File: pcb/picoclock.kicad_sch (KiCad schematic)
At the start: 67 parts, among them J1 UART, J10 USB, J11 Alt Power, J12 PWM, J13 AUDIO, J2 AUDIO, J3 xx, J4 xx, J5 Micro_SD_Card_Det1, J6 USB_C_Receptacle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

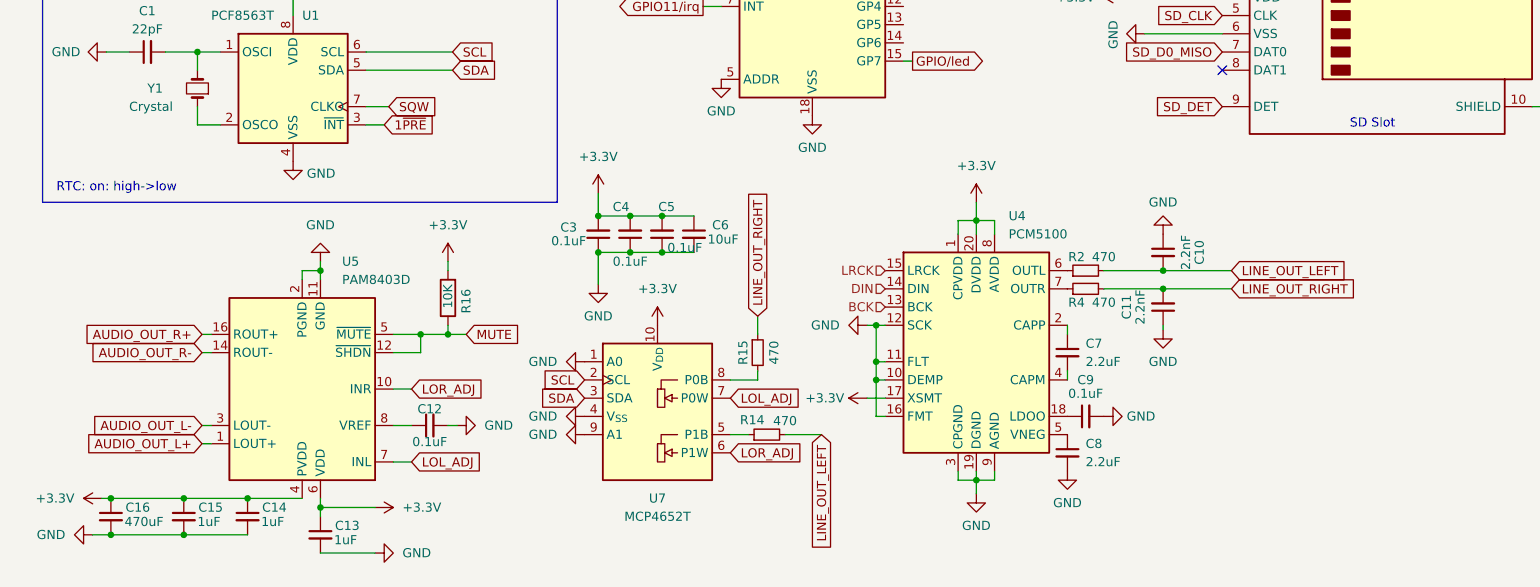
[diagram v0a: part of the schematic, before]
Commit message: [pcb] audio circuit fixes
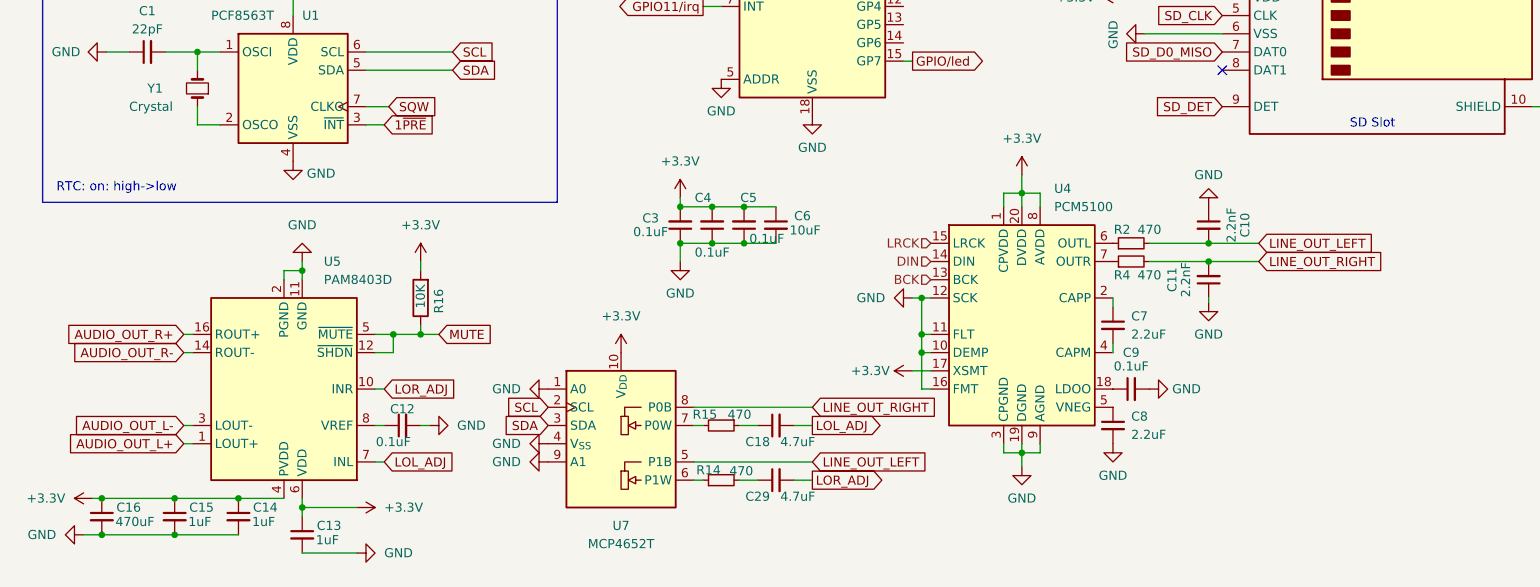
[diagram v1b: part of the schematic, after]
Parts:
- added C18, C29: 4.7uF, Capacitor_SMD:C_0603_1608Metric, symbol Device:C_Small
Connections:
- net LINE_OUT_LEFT: now also U7.5 (P1B); no longer R14.2
- net LINE_OUT_RIGHT: now also U7.8 (P0B); no longer R15.1
- net LOL_ADJ: now also C18.2; no longer U7.7 (P0W)
- net LOR_ADJ: now also C29.2; no longer U7.6 (P1W)
- net at R15.2: now also U7.7 (P0W); no longer U7.8 (P0B)
- net at R14.1: now also U7.6 (P1W); no longer U7.5 (P1B)
- new net: C18.1, R15.1
- new net: C29.1, R14.2
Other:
- moved on the sheet: C10, C11, C12, C13, C14, C15, C16, C3, C4, C5, C6, C7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

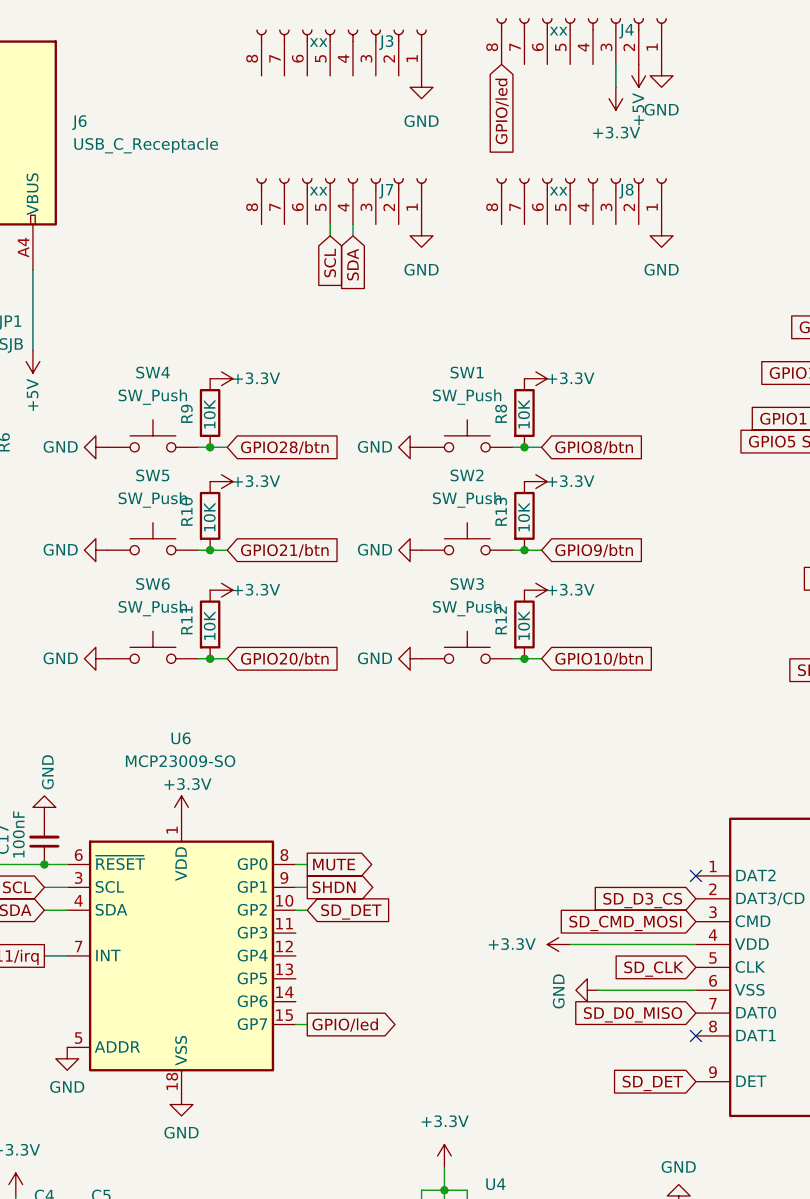
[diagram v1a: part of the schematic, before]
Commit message: [pcb] fpc screen connector at the right place
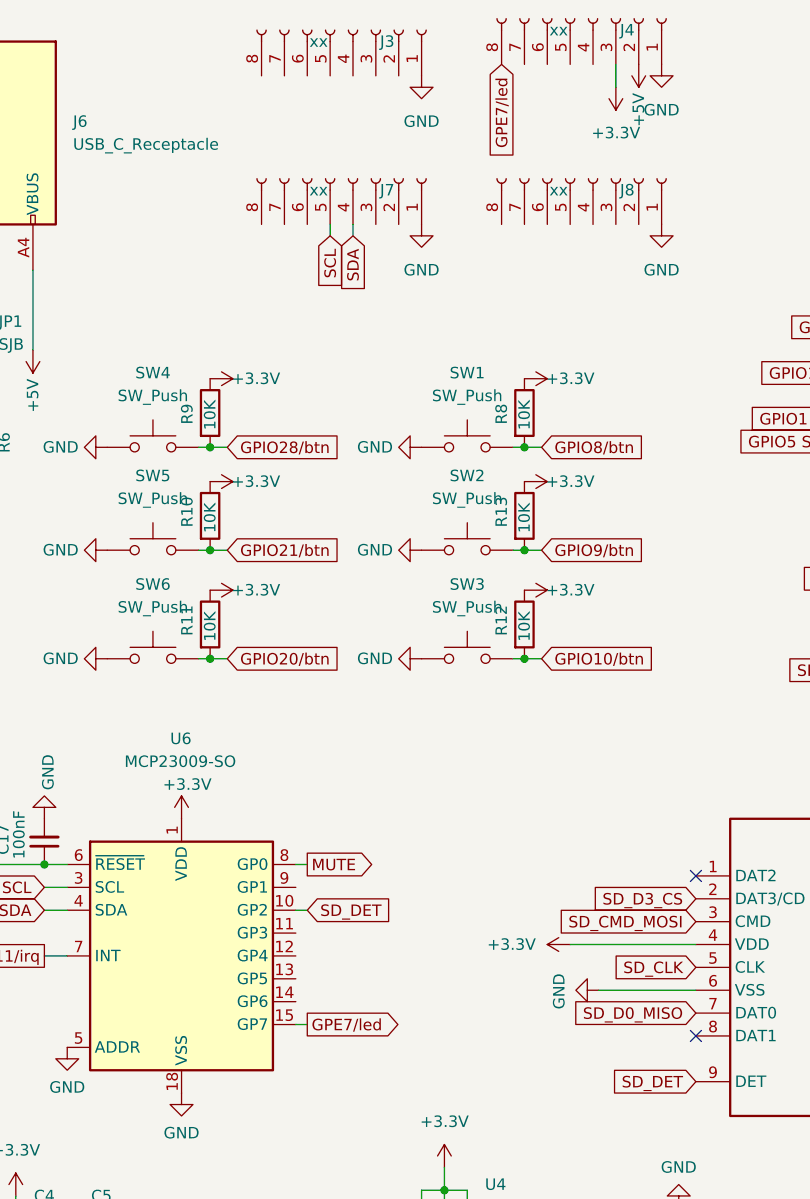
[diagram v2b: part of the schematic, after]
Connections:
- net GPIO/led renamed GPE7/led
- net SHDN: no longer names the net of U6.9 (GP1)
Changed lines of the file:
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@@
-	(wire
-		(pts
-			(xy 135.89 110.49) (xy 134.62 110.49)
-		)
-		(stroke
-			(width 0)
-			(type default)
-		)
-	)
 	(wire
 		(pts
@@
 		)
 	)
-	(global_label "GPIO{slash}led"
+	(global_label "GPE7{slash}led"
 		(shape output)
 		(at 135.89 125.73 0)
@@
 		)
 		(property "Intersheetrefs" "${INTERSHEET_REFS}"
-			(at 147.5838 125.73 0)
+			(at 148.007 125.73 0)
 			(effects
 				(font
@@
 		)
 	)
-	(global_label "GPIO{slash}led"
+	(global_label "GPE7{slash}led"
 		(shape input)
 		(at 157.48 19.05 270)
@@
 		)
 		(property "Intersheetrefs" "${INTERSHEET_REFS}"
-			(at 157.48 30.7438 90)
+			(at 157.48 31.167 90)
 			(effects
 				(font
@@
 			(effects
 				(font
-					(size 1.27 1.27)
-				)
-				(justify left)
-				(hide yes)
-			)
-		)
-	)
-	(global_label "SHDN"
-		(shape output)
-		(at 135.89 110.49 0)
-		(fields_autoplaced yes)
-		(effects
-			(font
-				(size 1.27 1.27)
-			)
-			(justify left)
-		)
-		(property "Intersheetrefs" "${INTERSHEET_REFS}"
-			(at 144.0157 110.49 0)
-			(effects
-				(font

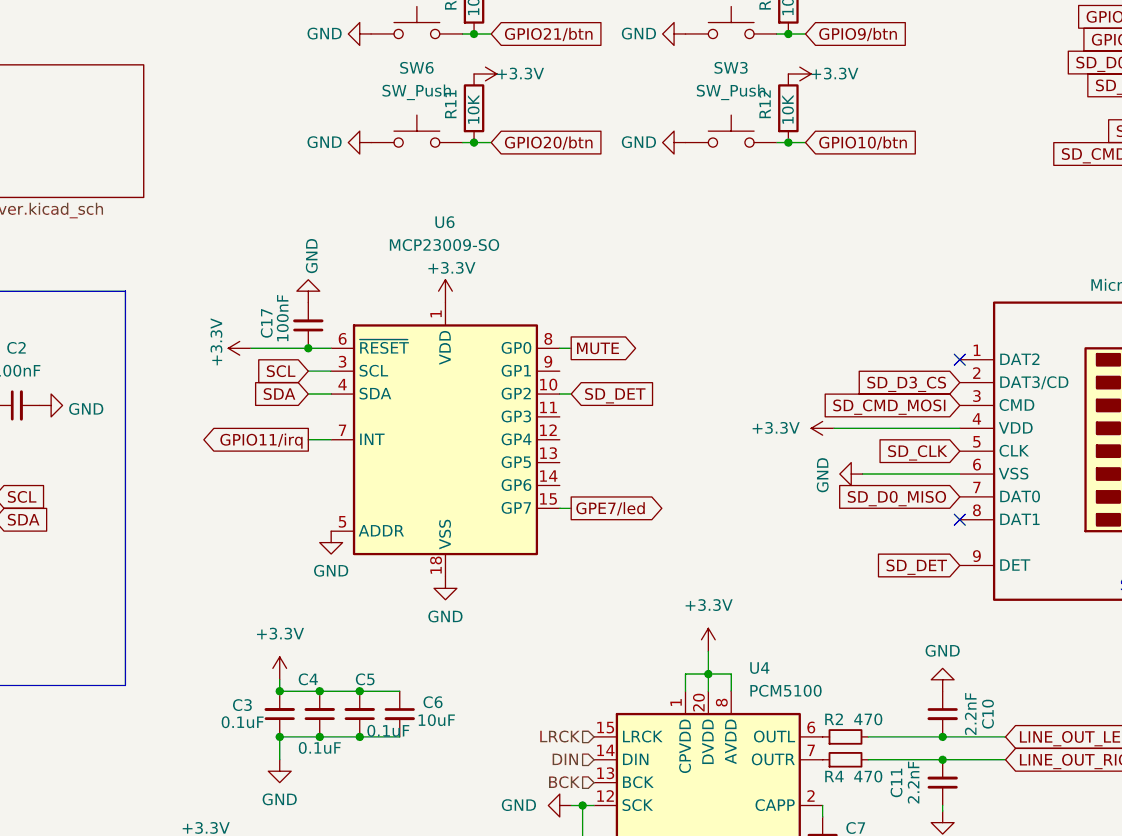
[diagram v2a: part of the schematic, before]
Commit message: [pcb] fixes for mcp23009 (bad footprint)
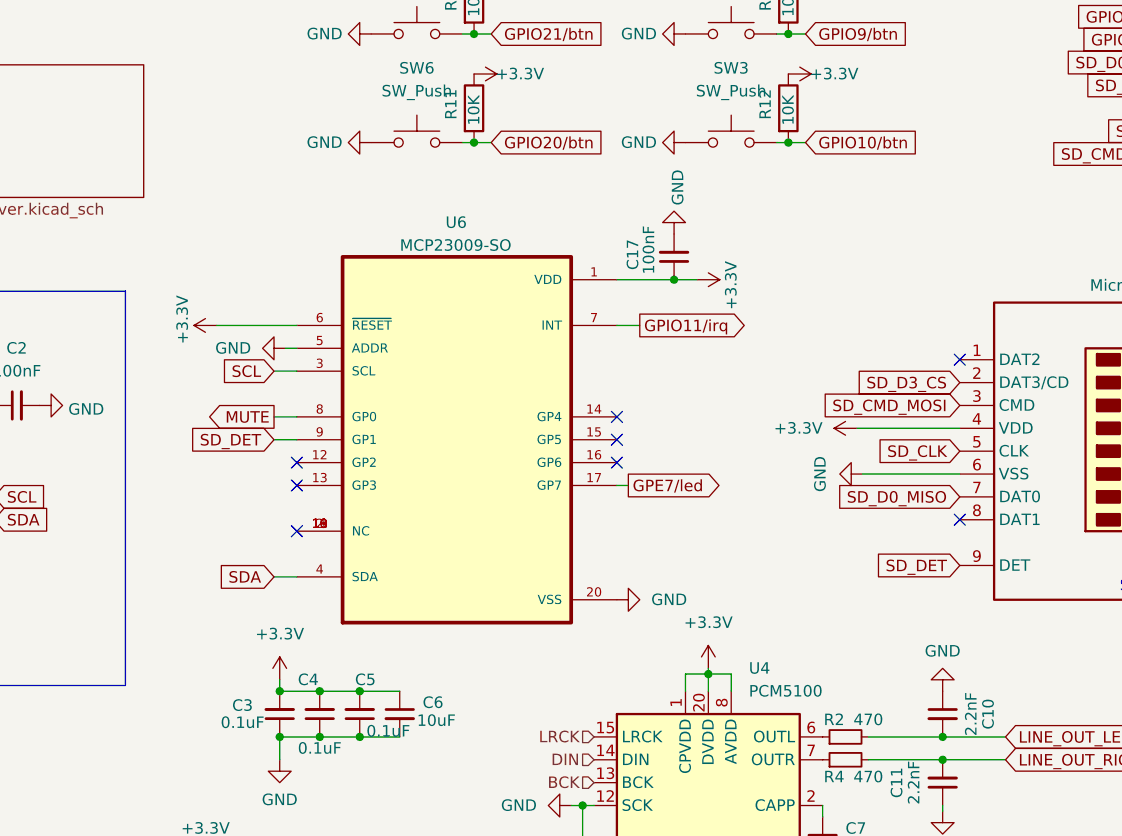
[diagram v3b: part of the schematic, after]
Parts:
- U6: symbol MCP23009-E_SO:MCP23009-SO -> MCP23009:MCP23009-E_SS; Availability (none) -> In Stock; Check_prices (none) -> https://www.snapeda.com/parts/MCP23009-E/SS/Microchip/view-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; Description_1 (none) -> Microchip MCP23009-E/SS, 8-channel 8bit I/O Expander 3.4MHz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; MANUFACTURER (none) -> Microchip; MAXIMUM_PACKAGE_HEIGHT (none) -> 2 mm; MF (none) -> Microchip; MP (none) -> MCP23009-E/SS; PARTREV (none) -> C; Package (none) -> SSOP-20 Microchip; Price (none) -> None; STANDARD (none) -> IPC 7351B; SnapEDA_Link (none) -> https://www.snapeda.com/parts/MCP23009-E/SS/Microchip/view-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
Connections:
- net GND: now also U6.20 (VSS); no longer U6.18 (VSS)
- net GPE7/led: now also U6.17 (GP7); no longer U6.15 (GP7)
- net SD_DET: now also U6.9 (GP1); no longer U6.10 (GP2)
- net at U6.11 (NC): now also U6.10 (NC), U6.18 (NC), U6.19 (NC), U6.2 (NC)
- no-connect marks 7 -> 13
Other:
- moved on the sheet: C17

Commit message: [pcb] add pullup resistor for MCP23009
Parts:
- added R17: 10K, Resistor_SMD:R_0603_1608Metric, symbol Device:R
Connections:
- net +3.3V: now also R17.1
- net GPE7/led: now also R17.2
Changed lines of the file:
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@@
 	)
 	(junction
+		(at 143.51 123.19)
+		(diameter 0)
+		(color 0 0 0 0)
+	)
+	(junction
 		(at 177.165 151.13)
 		(diameter 0)
@@
 	(wire
 		(pts
+			(xy 143.51 123.19) (xy 146.05 123.19)
+		)
+		(stroke
+			(width 0)
+			(type default)
+		)
+	)
+	(wire
+		(pts
 			(xy 21.59 186.69) (xy 22.86 186.69)
 		)
@@
 	(wire
 		(pts
+			(xy 143.51 123.19) (xy 140.97 123.19)
+		)
+		(stroke
+			(width 0)
+			(type default)
+		)
+	)
+	(wire
+		(pts
 			(xy 246.38 55.88) (xy 240.03 55.88)
 		)
@@
 	(wire
 		(pts
+			(xy 144.78 132.08) (xy 143.51 132.08)
+		)
+		(stroke
+			(width 0)
+			(type default)
+		)
+	)
+	(wire
+		(pts
 			(xy 160.02 85.09) (xy 158.75 85.09)
 		)
@@
 	(wire
 		(pts
+			(xy 143.51 132.08) (xy 143.51 130.81)
+		)
+		(stroke
+			(width 0)
+			(type default)
+		)
+	)
+	(wire
+		(pts
 			(xy 22.225 72.39) (xy 25.4 72.39)
 		)
@@
 	(wire
 		(pts
-			(xy 142.24 123.19) (xy 140.97 123.19)
-		)
-		(stroke
-			(width 0)
-			(type default)
-		)
-	)
-	(wire
-		(pts
 			(xy 20.32 191.77) (xy 22.86 191.77)
 		)
@@
 	(global_label "GPE7{slash}led"
 		(shape output)
-		(at 142.24 123.19 0)
+		(at 146.05 123.19 0)
 		(fields_autoplaced yes)
 		(effects
@@
 		)
 		(property "Intersheetrefs" "${INTERSHEET_REFS}"
-			(at 154.357 123.19 0)
+			(at 158.167 123.19 0)
 			(effects
 				(font
@@
 	)
 	(symbol
+		(lib_id "power:+3.3V")
+		(at 144.78 132.08 270)
+		(unit 1)
+		(exclude_from_sim no)
+		(in_bom yes)
+		(on_board yes)
+		(dnp no)
+		(property "Reference" "#PWR075"
+			(at 140.97 132.08 0)
+			(effects
+				(font
+					(size 1.27 1.27)
+				)
+				(hide yes)
+			)
+		)
+		(property "Value" "+3.3V"
+			(at 149.86 132.08 0)
+			(effects
+				(font
+					(size 1.27 1.27)
+				)
+			)
+		)
+		(property "Footprint" ""
+			(at 144.78 132.08 0)
+			(effects
+				(font
+					(size 1.27 1.27)
+				)
+				(hide yes)
+			)
+		)
+		(property "Datasheet" ""
+			(at 144.78 132.08 0)
+			(effects
+				(font
+					(size 1.27 1.27)
+				)
+				(hide yes)
+			)
+		)
+		(property "Description" ""
+			(at 144.78 132.08 0)
+			(effects
+				(font
+					(size 1.27 1.27)
+				)
+				(hide yes)
+			)
+		)
+		(pin "1"
+		)
+		(instances
+			(project "picoclock"
+				(path "/3b9dec0e-e0b7-4565-afc9-c4692f41aea9"
+					(reference "#PWR075")
+					(unit 1)
+				)
+			)
+		)
+	)
+	(symbol
 		(lib_id "Mechanical:MountingHole_Pad")
 		(at 22.86 40.64 0)
@@
 					(unit 1)
 				)
+			)
+		)
+	)
+	(symbol
+		(lib_id "Device:R")
+		(at 143.51 127 180)
+		(unit 1)
+		(exclude_from_sim no)
+		(in_bom yes)
+		(on_board yes)
+		(dnp no)
+		(property "Reference" "R17"
+			(at 146.05 125.73 90)
+			(effects
+				(font
+					(size 1.27 1.27)
+				)
+				(justify left)
+			)
+		)
+		(property "Value" "10K"
+			(at 143.51 125.095 90)
+			(effects
+				(font
+					(size 1.27 1.27)
+				)
+				(justify left)
+			)
+		)
+		(property "Footprint" "Resistor_SMD:R_0603_1608Metric"
+			(at 145.288 127 90)
+			(effects
+				(font
+					(size 1.27 1.27)
+				)
+				(hide yes)
+			)
+		)
+		(property "Datasheet" "~"
+			(at 143.51 127 0)
+			(effects
+				(font
+					(size 1.27 1.27)
+				)
+				(hide yes)
+			)
+		)
+		(property "Description" ""
+			(at 143.51 127 0)
+			(effects
+				(font
+					(size 1.27 1.27)
+				)
+				(hide yes)
+			)
+		)
+		(property "LCSC" "C25744"
+			(at 143.51 127 0)
+			(effects
+				(font
+					(size 1.27 1.27)
+				)
+				(hide yes)
+			)
+		)
+		(pin "1"
+		)
+		(pin "2"
+		)
+		(instances
+			(project "picoclock"
+				(path "/3b9dec0e-e0b7-4565-afc9-c4692f41aea9"
+					(reference "R17")
+					(unit 1)
+				)
